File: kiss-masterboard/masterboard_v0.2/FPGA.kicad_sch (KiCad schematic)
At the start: 89 parts, among them J10 CRESET, J11 Jumper, J12 Jumper, J13 Conn_02x08_Odd_Even, J14 Conn_02x08_Odd_Even, J15 jmp, J16 jmp, J8 Jumper, U11 TLV75733PDBV, U13 SN74LVC8T245, U14 W25Q, U17 12MHz, U2 SN74LVC8T245, U4 ICE40UP5k-SG48, U5 SN74LVC8T245, U8 TLV75709PDBV

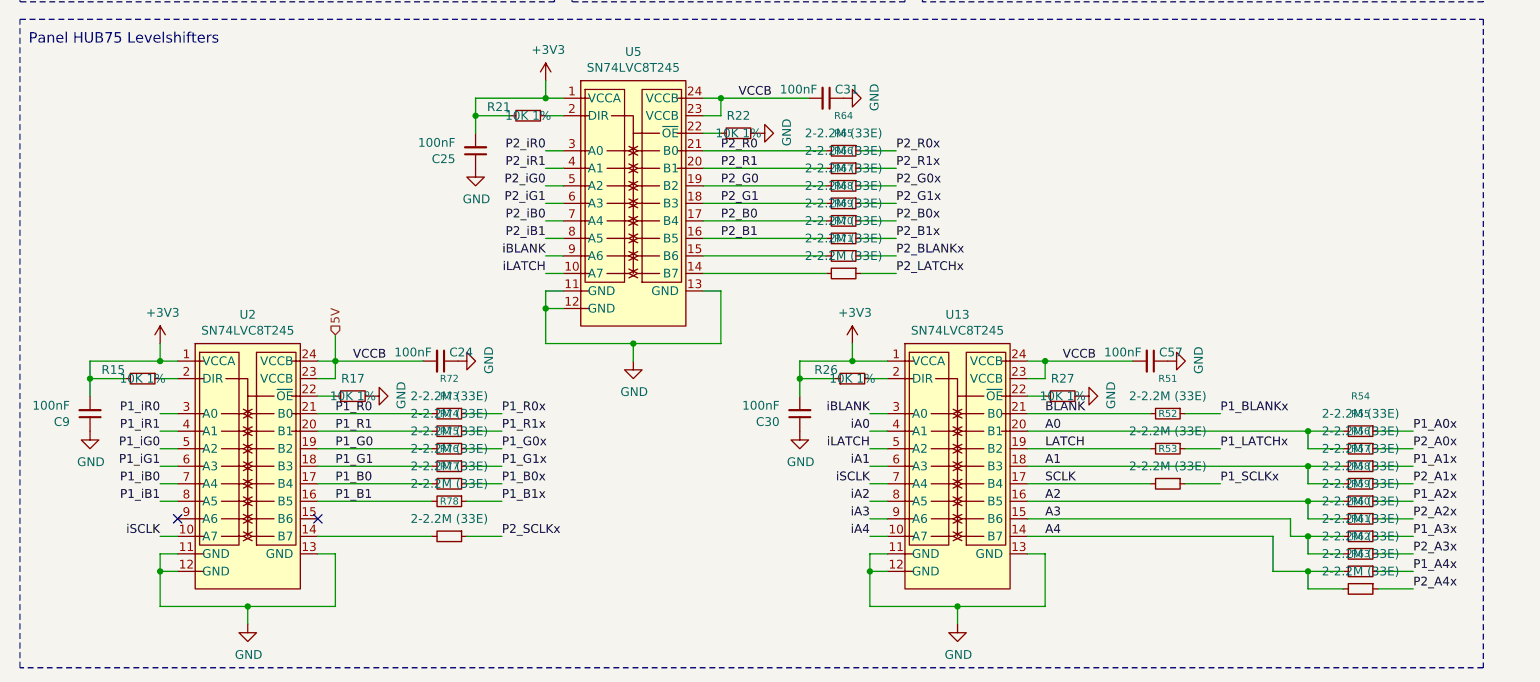
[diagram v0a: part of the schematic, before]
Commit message: kiss-masterboard: fix R51-R78 value, was 2.2M instead of 33E
R51-R78 (HUB75 LATCH/SCLK/BLANK/A0-A4/RGB data series resistors for
both panel connectors) were populated with 2-2.2M instead of the
intended 33E - a BOM/kitting error. 2.2M in series with these
CMOS-input lines low-pass filters the edges far too slowly for HUB75
timing at any usable clock, making the display unusable regardless of
gateware. Confirmed and hand-reworked on the physical board; corrected
here so the next fab run stuffs 33E instead of repeating the error.

Added a note next to the "Panel HUB75 Levelshifters" section
documenting this, and the related U17 (12MHz oscillator) fix.
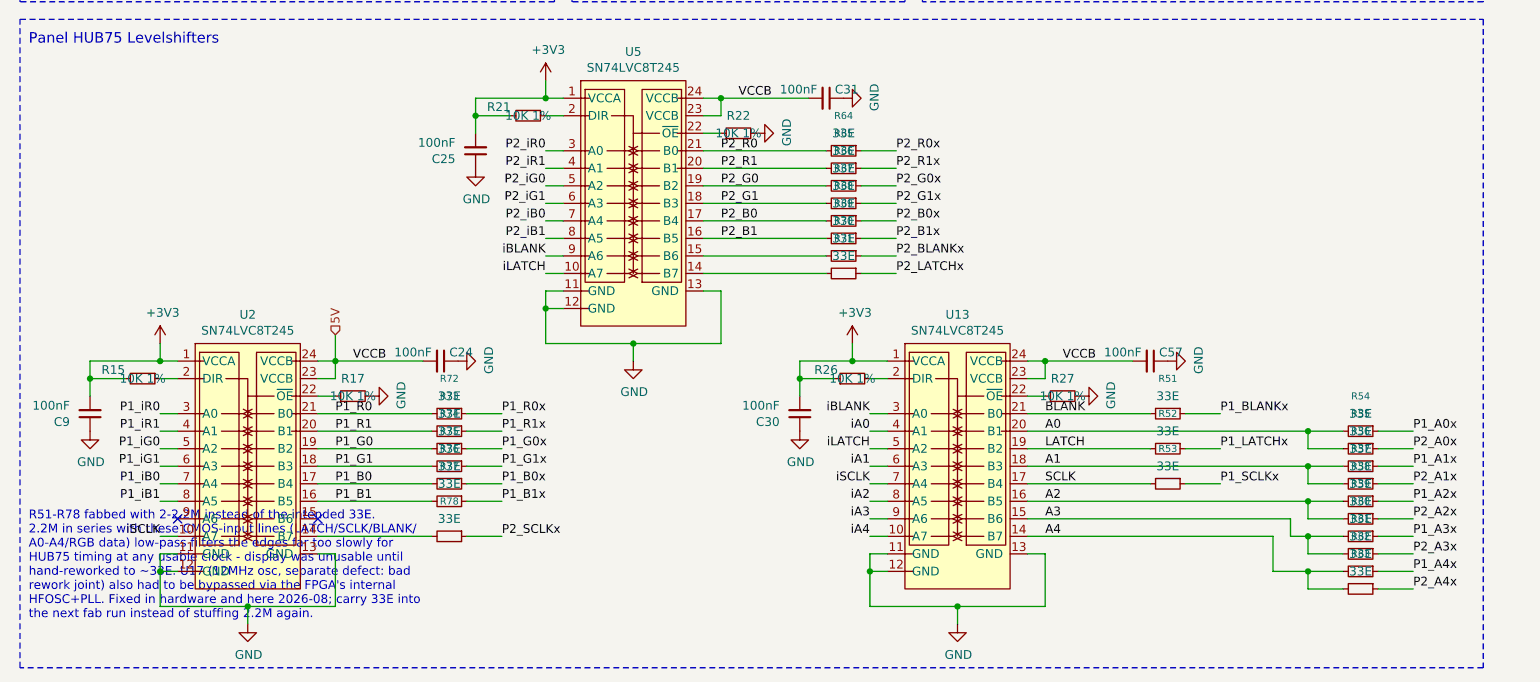
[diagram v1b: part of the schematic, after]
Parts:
- R51, R52, R53, R54, R55, R56, R57, R58, R59, R60, R61, R62, R63, R64, R65, R66, R67, R68, R69, R70, R71, R72, R73, R74, R75, R76, R77, R78: value 2-2.2M (33E) -> 33E
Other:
- note added: "R51-R78 fabbed with 2-2.2M instead of the intended 33E. 2.2M in series with these CMOS-input lines (LATCH/SCLK/BLANK/ A0-A4/RGB data) low-pass filters the edges far too slowly for HUB75 timing at any usable clock - display was unusable until hand-reworked to ~33E. U17 (12MHz osc, separate defect: bad rework joint) also had to be bypassed via the FPGA's internal HFOSC+PLL. Fixed in hardware and he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"
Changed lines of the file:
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@@
 		)
 	)
+	(text "R51-R78 fabbed with 2-2.2M instead of the intended 33E.
+2.2M in series with these CMOS-input lines (LATCH/SCLK/BLANK/
+A0-A4/RGB data) low-pass filters the edges far too slowly for
+HUB75 timing at any usable clock - display was unusable until
+hand-reworked to ~33E. U17 (12MHz osc, separate defect: bad
+rework joint) also had to be bypassed via the FPGA's internal
+HFOSC+PLL. Fixed in hardware and here 2026-08; carry 33E into
+the next fab run instead of stuffing 2.2M again."
+		(exclude_from_sim no)
+		(at 16.51 275.0 0)
+		(effects
+			(font
+				(size 1.27 1.27)
+			)
+			(justify left bottom)
+		)
+	)
 	(text "DPair"
 		(exclude_from_sim no)
@@
 			)
 		)
-		(property "Value" "2-2.2M (33E)"
+		(property "Value" "33E"
 			(at 209.55 262.89 90)
 			(show_name no)
@@
 			)
 		)
-		(property "Value" "2-2.2M (33E)"
+		(property "Value" "33E"
 			(at 134.62 217.17 90)
 			(show_name no)
@@
 			)
 		)
-		(property "Value" "2-2.2M (33E)"
+		(property "Value" "33E"
 			(at 181.61 242.57 90)
 			(show_name no)
@@
 			)
 		)
-		(property "Value" "2-2.2M (33E)"
+		(property "Value" "33E"
 			(at 77.47 252.73 90)
 			(show_name no)
@@
 			)
 		)
-		(property "Value" "2-2.2M (33E)"
+		(property "Value" "33E"
 			(at 209.55 247.65 90)
 			(show_name no)
@@
 			)
 		)
-		(property "Value" "2-2.2M (33E)"
+		(property "Value" "33E"
 			(at 209.55 265.43 90)
 			(show_name no)
@@
 			)
 		)
-		(property "Value" "2-2.2M (33E)"
+		(property "Value" "33E"
 			(at 77.47 255.27 90)
 			(show_name no)
@@
 			)
 		)
-		(property "Value" "2-2.2M (33E)"
+		(property "Value" "33E"
 			(at 134.62 222.25 90)
 			(show_name no)
@@
 			)
 		)
-		(property "Value" "2-2.2M (33E)"
+		(property "Value" "33E"
 			(at 77.47 247.65 90)
 			(show_name no)
@@
 			)
 		)
-		(property "Value" "2-2.2M (33E)"
+		(property "Value" "33E"
 			(at 209.55 267.97 90)
 			(show_name no)
@@
 			)
 		)
-		(property "Value" "2-2.2M (33E)"
+		(property "Value" "33E"
 			(at 134.62 209.55 90)
 			(show_name no)
@@
 			)
 		)
-		(property "Value" "2-2.2M (33E)"
+		(property "Value" "33E"
 			(at 134.62 214.63 90)
 			(show_name no)
@@
 			)
 		)
-		(property "Value" "2-2.2M (33E)"
+		(property "Value" "33E"
 			(at 134.62 212.09 90)
 			(show_name no)
@@
 			)
 		)
-		(property "Value" "2-2.2M (33E)"
+		(property "Value" "33E"
 			(at 209.55 257.81 90)
 			(show_name no)
@@
 			)
 		)
-		(property "Value" "2-2.2M (33E)"
+		(property "Value" "33E"
 			(at 134.62 219.71 90)
 			(show_name no)
@@
 			)
 		)
-		(property "Value" "2-2.2M (33E)"
+		(property "Value" "33E"
 			(at 209.55 250.19 90)
 			(show_name no)
@@
 			)
 		)
-		(property "Value" "2-2.2M (33E)"
+		(property "Value" "33E"
 			(at 77.47 260.35 90)
 			(show_name no)
@@
 			)
 		)
-		(property "Value" "2-2.2M (33E)"
+		(property "Value" "33E"
 			(at 209.55 245.11 90)
 			(show_name no)
@@
 			)
 		)
-		(property "Value" "2-2.2M (33E)"
+		(property "Value" "33E"
 			(at 77.47 250.19 90)
 			(show_name no)
@@
 			)
 		)
-		(property "Value" "2-2.2M (33E)"
+		(property "Value" "33E"
 			(at 209.55 255.27 90)
 			(show_name no)
@@
 			)
 		)
-		(property "Value" "2-2.2M (33E)"
+		(property "Value" "33E"
 			(at 134.62 204.47 90)
 			(show_name no)
@@
 			)
 		)
-		(property "Value" "2-2.2M (33E)"
+		(property "Value" "33E"
 			(at 209.55 260.35 90)
 			(show_name no)
@@
 			)
 		)
-		(property "Value" "2-2.2M (33E)"
+		(property "Value" "33E"
 			(at 209.55 252.73 90)
 			(show_name no)
@@
 			)
 		)
-		(property "Value" "2-2.2M (33E)"
+		(property "Value" "33E"
 			(at 77.47 242.57 90)
 			(show_name no)
@@
 			)
 		)
-		(property "Value" "2-2.2M (33E)"
+		(property "Value" "33E"
 			(at 181.61 252.73 90)
 			(show_name no)
@@
 			)
 		)
-		(property "Value" "2-2.2M (33E)"
+		(property "Value" "33E"
 			(at 77.47 245.11 90)
 			(show_name no)
@@
 			)
 		)
-		(property "Value" "2-2.2M (33E)"
+		(property "Value" "33E"
 			(at 134.62 207.01 90)
 			(show_name no)
@@
 			)
 		)
-		(property "Value" "2-2.2M (33E)"
+		(property "Value" "33E"
 			(at 181.61 247.65 90)
 			(show_name no)

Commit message: Revert "kiss-masterboard: fix R51-R78 value, was 2.2M instead of 33E"
This reverts commit be2e0cd53d49abef9a9fc2547556a5b37668e0ac.
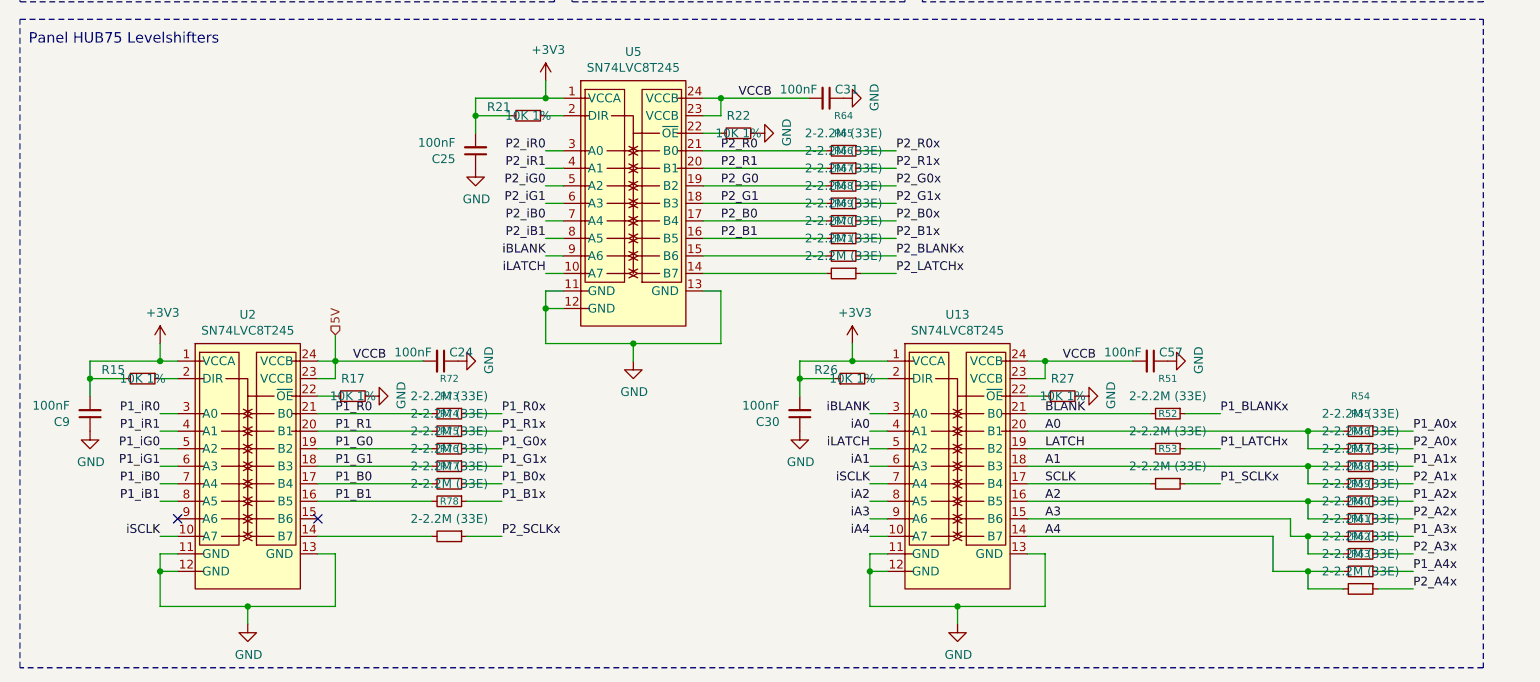
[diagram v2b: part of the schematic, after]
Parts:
- R51, R52, R53, R54, R55, R56, R57, R58, R59, R60, R61, R62, R63, R64, R65, R66, R67, R68, R69, R70, R71, R72, R73, R74, R75, R76, R77, R78: value 33E -> 2-2.2M (33E)
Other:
- note removed: "R51-R78 fabbed with 2-2.2M instead of the intended 33E. 2.2M in series with these CMOS-input lines (LATCH/SCLK/BLANK/ A0-A4/RGB data) low-pass filters the edges far too slowly for HUB75 timing at any usable clock - display was unusable until hand-reworked to ~33E. U17 (12MHz osc, separate defect: bad rework joint) also had to be bypassed via the FPGA's internal HFOSC+PLL. Fixed in hardware and he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"
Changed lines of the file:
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@@
 		)
 	)
-	(text "R51-R78 fabbed with 2-2.2M instead of the intended 33E.
-2.2M in series with these CMOS-input lines (LATCH/SCLK/BLANK/
-A0-A4/RGB data) low-pass filters the edges far too slowly for
-HUB75 timing at any usable clock - display was unusable until
-hand-reworked to ~33E. U17 (12MHz osc, separate defect: bad
-rework joint) also had to be bypassed via the FPGA's internal
-HFOSC+PLL. Fixed in hardware and here 2026-08; carry 33E into
-the next fab run instead of stuffing 2.2M again."
-		(exclude_from_sim no)
-		(at 16.51 275.0 0)
-		(effects
-			(font
-				(size 1.27 1.27)
-			)
-			(justify left bottom)
-		)
-	)
 	(text "DPair"
 		(exclude_from_sim no)
@@
 			)
 		)
-		(property "Value" "33E"
+		(property "Value" "2-2.2M (33E)"
 			(at 209.55 262.89 90)
 			(show_name no)
@@
 			)
 		)
-		(property "Value" "33E"
+		(property "Value" "2-2.2M (33E)"
 			(at 134.62 217.17 90)
 			(show_name no)
@@
 			)
 		)
-		(property "Value" "33E"
+		(property "Value" "2-2.2M (33E)"
 			(at 181.61 242.57 90)
 			(show_name no)
@@
 			)
 		)
-		(property "Value" "33E"
+		(property "Value" "2-2.2M (33E)"
 			(at 77.47 252.73 90)
 			(show_name no)
@@
 			)
 		)
-		(property "Value" "33E"
+		(property "Value" "2-2.2M (33E)"
 			(at 209.55 247.65 90)
 			(show_name no)
@@
 			)
 		)
-		(property "Value" "33E"
+		(property "Value" "2-2.2M (33E)"
 			(at 209.55 265.43 90)
 			(show_name no)
@@
 			)
 		)
-		(property "Value" "33E"
+		(property "Value" "2-2.2M (33E)"
 			(at 77.47 255.27 90)
 			(show_name no)
@@
 			)
 		)
-		(property "Value" "33E"
+		(property "Value" "2-2.2M (33E)"
 			(at 134.62 222.25 90)
 			(show_name no)
@@
 			)
 		)
-		(property "Value" "33E"
+		(property "Value" "2-2.2M (33E)"
 			(at 77.47 247.65 90)
 			(show_name no)
@@
 			)
 		)
-		(property "Value" "33E"
+		(property "Value" "2-2.2M (33E)"
 			(at 209.55 267.97 90)
 			(show_name no)
@@
 			)
 		)
-		(property "Value" "33E"
+		(property "Value" "2-2.2M (33E)"
 			(at 134.62 209.55 90)
 			(show_name no)
@@
 			)
 		)
-		(property "Value" "33E"
+		(property "Value" "2-2.2M (33E)"
 			(at 134.62 214.63 90)
 			(show_name no)
@@
 			)
 		)
-		(property "Value" "33E"
+		(property "Value" "2-2.2M (33E)"
 			(at 134.62 212.09 90)
 			(show_name no)
@@
 			)
 		)
-		(property "Value" "33E"
+		(property "Value" "2-2.2M (33E)"
 			(at 209.55 257.81 90)
 			(show_name no)
@@
 			)
 		)
-		(property "Value" "33E"
+		(property "Value" "2-2.2M (33E)"
 			(at 134.62 219.71 90)
 			(show_name no)
@@
 			)
 		)
-		(property "Value" "33E"
+		(property "Value" "2-2.2M (33E)"
 			(at 209.55 250.19 90)
 			(show_name no)
@@
 			)
 		)
-		(property "Value" "33E"
+		(property "Value" "2-2.2M (33E)"
 			(at 77.47 260.35 90)
 			(show_name no)
@@
 			)
 		)
-		(property "Value" "33E"
+		(property "Value" "2-2.2M (33E)"
 			(at 209.55 245.11 90)
 			(show_name no)
@@
 			)
 		)
-		(property "Value" "33E"
+		(property "Value" "2-2.2M (33E)"
 			(at 77.47 250.19 90)
 			(show_name no)
@@
 			)
 		)
-		(property "Value" "33E"
+		(property "Value" "2-2.2M (33E)"
 			(at 209.55 255.27 90)
 			(show_name no)
@@
 			)
 		)
-		(property "Value" "33E"
+		(property "Value" "2-2.2M (33E)"
 			(at 134.62 204.47 90)
 			(show_name no)
@@
 			)
 		)
-		(property "Value" "33E"
+		(property "Value" "2-2.2M (33E)"
 			(at 209.55 260.35 90)
 			(show_name no)
@@
 			)
 		)
-		(property "Value" "33E"
+		(property "Value" "2-2.2M (33E)"
 			(at 209.55 252.73 90)
 			(show_name no)
@@
 			)
 		)
-		(property "Value" "33E"
+		(property "Value" "2-2.2M (33E)"
 			(at 77.47 242.57 90)
 			(show_name no)
@@
 			)
 		)
-		(property "Value" "33E"
+		(property "Value" "2-2.2M (33E)"
 			(at 181.61 252.73 90)
 			(show_name no)
@@
 			)
 		)
-		(property "Value" "33E"
+		(property "Value" "2-2.2M (33E)"
 			(at 77.47 245.11 90)
 			(show_name no)
@@
 			)
 		)
-		(property "Value" "33E"
+		(property "Value" "2-2.2M (33E)"
 			(at 134.62 207.01 90)
 			(show_name no)
@@
 			)
 		)
-		(property "Value" "33E"
+		(property "Value" "2-2.2M (33E)"
 			(at 181.61 247.65 90)
 			(show_name no)
